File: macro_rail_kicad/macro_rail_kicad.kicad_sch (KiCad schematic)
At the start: 18 parts, among them J1 Battery, J2 Motor, J3 128x128 OLED, J4 GIMBAL, J5 2.5mm Plug, SW1 POWER, SW2 SHUTTER, SW3 PREVIOUS, SW4 NEXT, SW5 RESET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

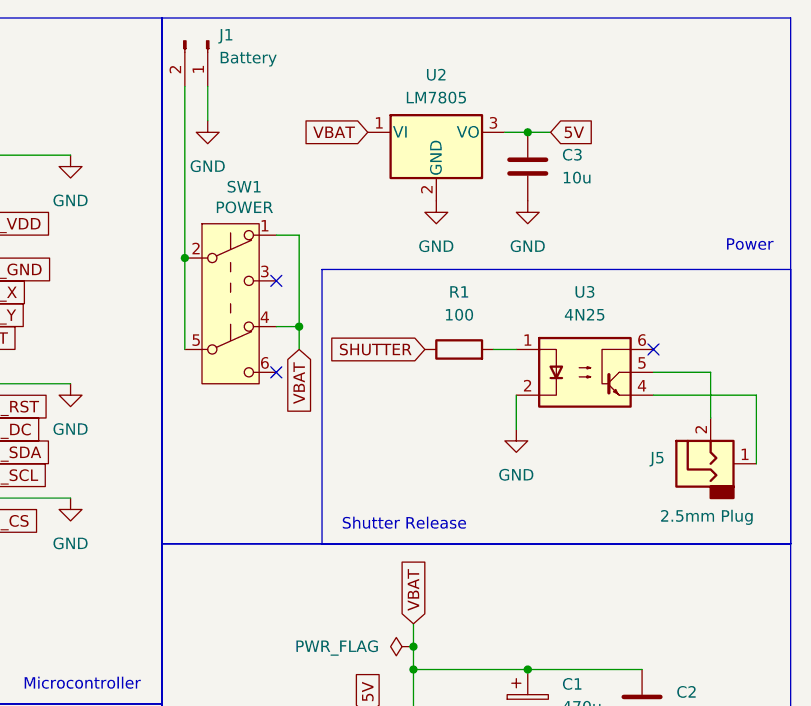
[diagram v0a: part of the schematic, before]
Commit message: README links updates.  Removed power switch (amps too low)
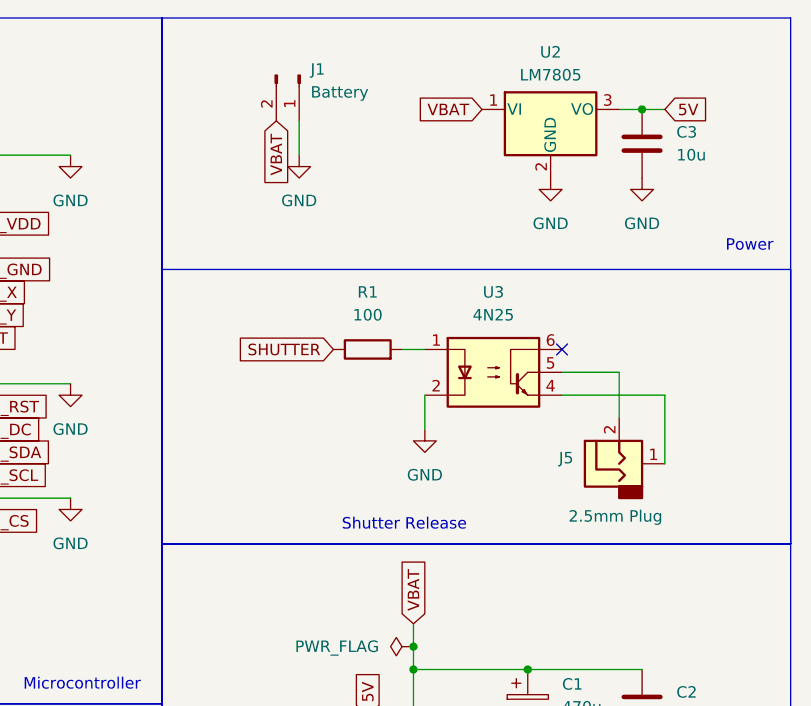
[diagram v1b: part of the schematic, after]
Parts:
- removed SW1: POWER, Button_Switch_THT:SW_Push_2P2T_Toggle_CK_PVA2OAH5xxxxxxV2, symbol Switch:SW_Push_DPDT
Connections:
- net VBAT: now also J1.2 (Pin_2)
- no-connect marks 18 -> 16
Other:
- moved on the sheet: C3, J1, J5, R1, U2, U3

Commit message: Updated schmatic and pcb for microstepping
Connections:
- net 5V: now also A1.10 (MS1), A1.11 (MS2), A1.12 (MS3)
- net GND: no longer A1.10 (MS1), A1.11 (MS2), A1.12 (MS3)
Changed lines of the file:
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@@
-	)
-	(junction
-		(at 133.35 135.89)
-		(diameter 0)
-		(color 0 0 0 0)
 	)
 	(junction
@@
 		(color 0 0 0 0)
 	)
-	(junction
-		(at 143.51 135.89)
-		(diameter 0)
-		(color 0 0 0 0)
-	)
 	(no_connect
 		(at 96.52 34.29)
@@
 		(pts
 			(xy 133.35 121.92) (xy 130.81 121.92)
-		)
-		(stroke
-			(width 0)
-			(type default)
-		)
-	)
-	(wire
-		(pts
-			(xy 133.35 135.89) (xy 143.51 135.89)
 		)
 		(stroke
@@
 			(effects
 				(font
+					(size 1.27 1.27)
+				)
+				(justify right)
+				(hide yes)
+			)
+		)
+	)
+	(global_label "5V"
+		(shape input)
+		(at 130.81 135.89 270)
+		(fields_autoplaced yes)
+		(effects
+			(font
+				(size 1.27 1.27)
+			)
+			(justify right)
+		)
+		(property "Intersheetrefs" "${INTERSHEET_REFS}"
+			(at 130.81 141.1733 90)
+			(effects
+				(font
